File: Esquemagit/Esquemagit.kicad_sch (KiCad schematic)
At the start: 28 parts, among them J1 Conn_01x04_Pin, J2 UJ20-C-H-G-MSMT-9B-P16-TR, U1 LMV321, U2 AMS1117-3.3, U5 ESP32-WROOM-32

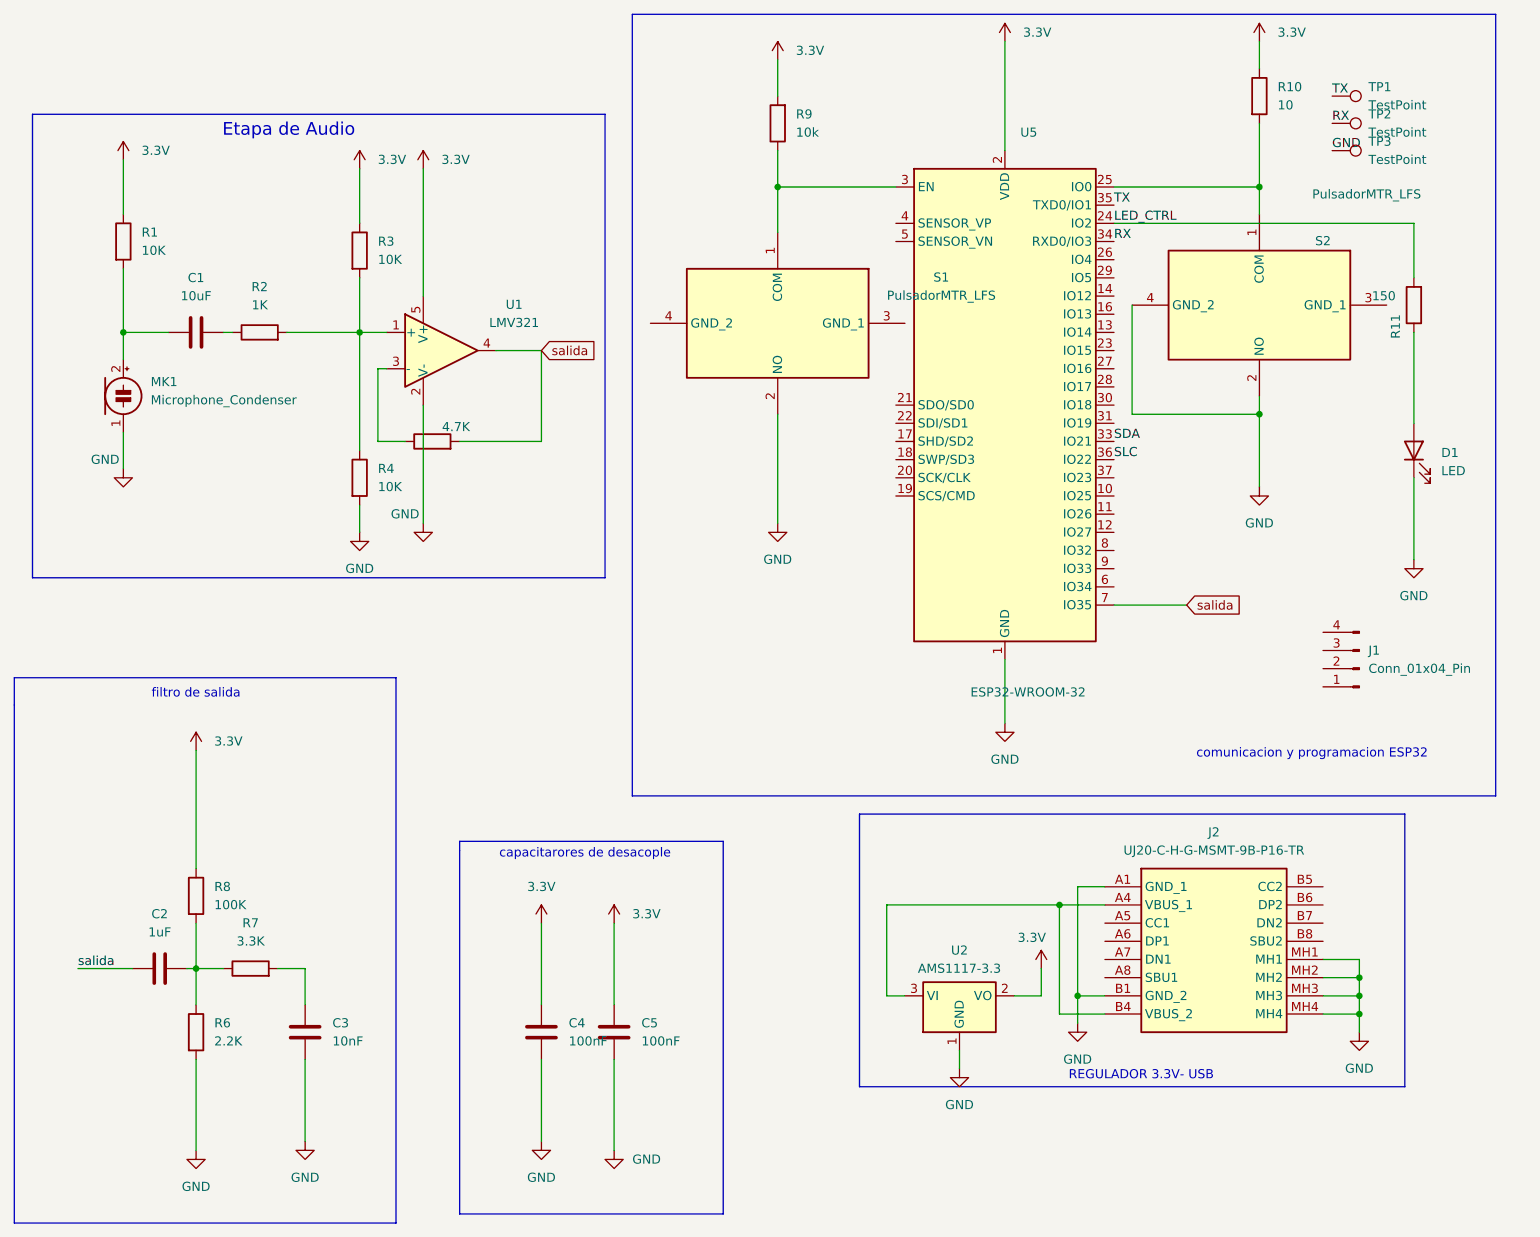
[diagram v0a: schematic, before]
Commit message: feat: pulsadores,usb c, huellas ,microfono digital
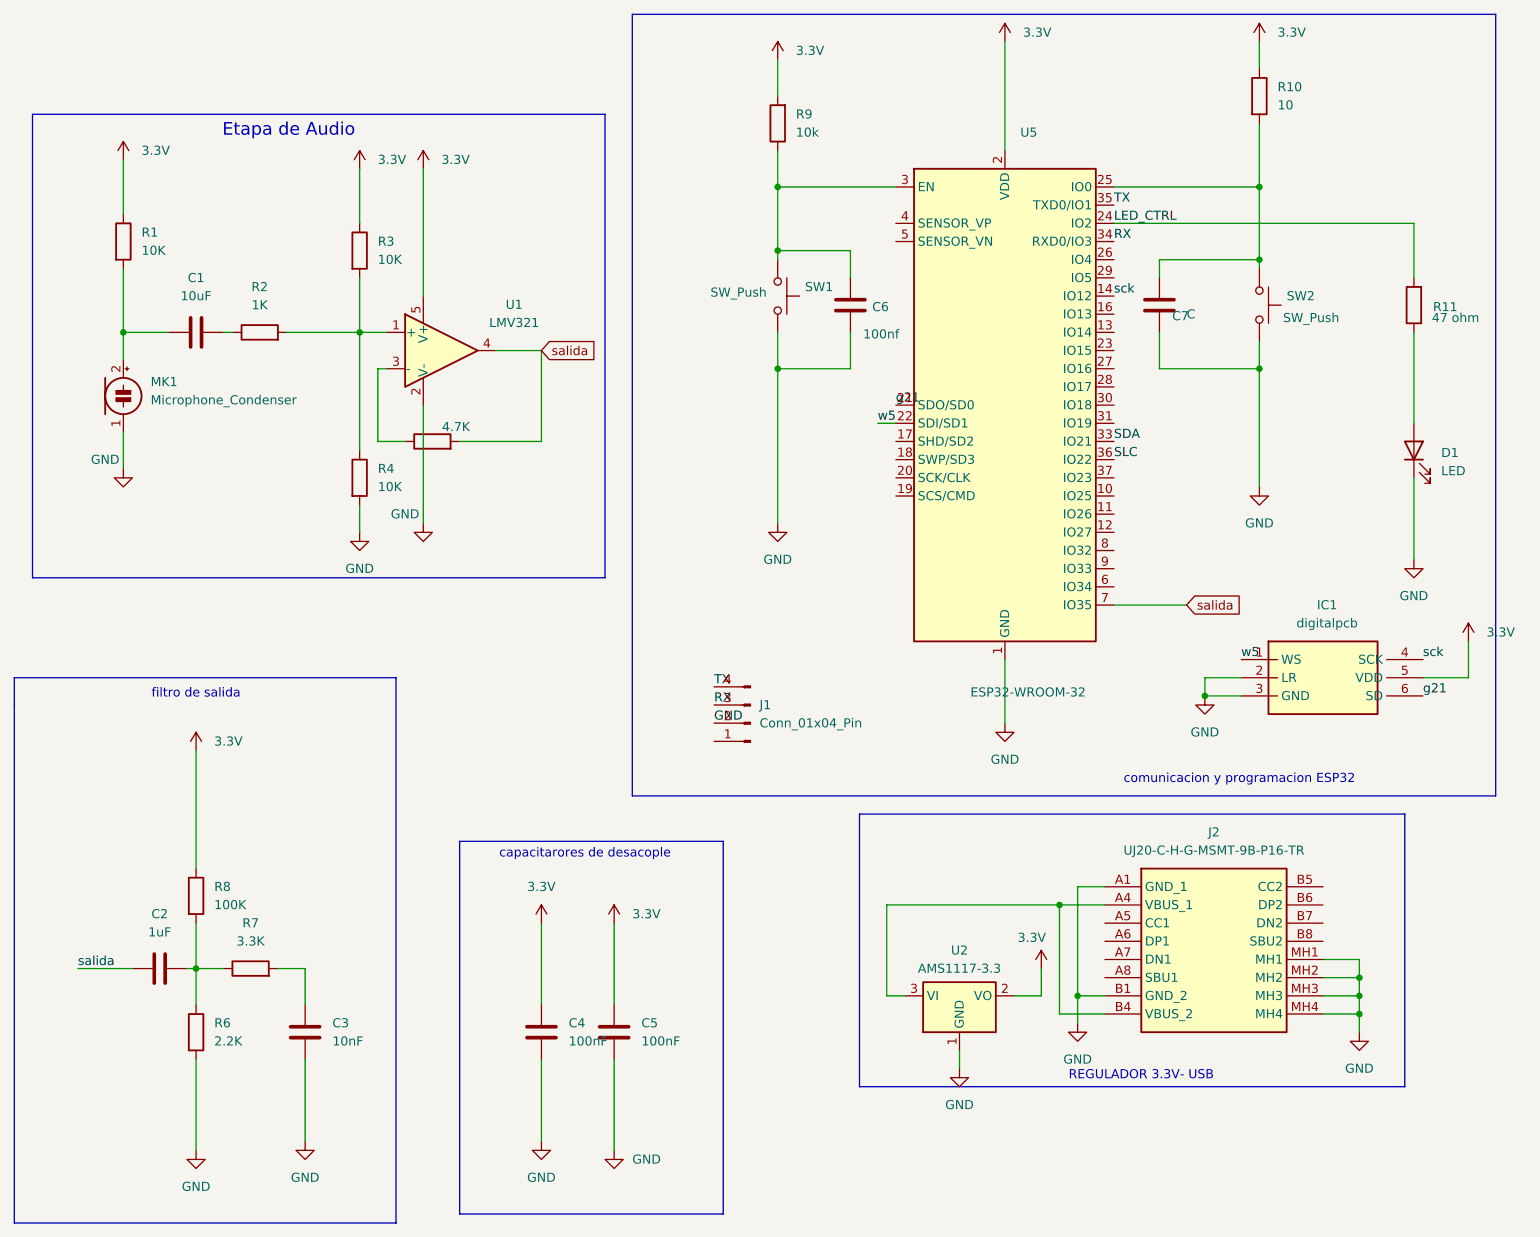
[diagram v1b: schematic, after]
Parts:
- removed S1, S2: PulsadorMTR_LFS, Button_Switch_SMD:SW_DIP_SPSTx02_Slide_6.7x6.64mm_W6.73mm_P2.54mm_LowProfile_JPin, symbol pulsador:PulsadorMTR_LFS
- removed TP1, TP2, TP3: TestPoint, TestPoint:TestPoint_Pad_D1.5mm, symbol Connector:TestPoint
- added C6: 100nf, Capacitor_SMD:C_0805_2012Metric, symbol Device:C
- added C7: C, symbol Device:C
- added IC1: digitalpcb, microfono.digital:ICS43434, symbol ICS-43434:digitalpcb
- added SW1, SW2: SW_Push, boton2:T6VJ11GQR, symbol Switch:SW_Push
- J2: footprint UJ20CHGMSMT9BP16TR -> usb.c2:UJ20CHGMSMT9BP16TR
- R11: value 150 -> 47 ohm
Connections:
- net 3.3V: now also IC1.5 (VDD)
- net GND: now also J1.2 (Pin_2), C6.2, C7.2, IC1.2 (LR), IC1.3 (GND), SW1.2, SW2.2
- net RX: now also J1.3 (Pin_3)
- net TX: now also J1.4 (Pin_4)
- net at R10.2, U5.25 (IO0): now also C7.1, SW2.1
- net at R9.1, U5.3 (EN): now also C6.1, SW1.1
- net sck: now reaches U5.14 (IO12)
- net sck: now also IC1.4 (SCK)
- net g21: now reaches U5.21 (SDO/SD0)
- net g21: now also IC1.6 (SD)
- net w5: now reaches U5.22 (SDI/SD1)
- net w5: now also IC1.1 (WS)
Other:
- moved on the sheet: J1

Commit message: feat: actualizaciones en el diseño del esquematico
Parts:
- SW1, SW2: footprint boton2:T6VJ11GQR -> Button_Switch_SMD:SW_Push_1TS009xxxx-xxxx-xxxx_6x6x5mm
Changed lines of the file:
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@@
 			)
 		)
-		(property "Footprint" "boton2:T6VJ11GQR"
+		(property "Footprint" "Button_Switch_SMD:SW_Push_1TS009xxxx-xxxx-xxxx_6x6x5mm"
 			(at 208.28 54.61 0)
 			(hide yes)
@@
 			)
 		)
-		(property "Footprint" "boton2:T6VJ11GQR"
+		(property "Footprint" "Button_Switch_SMD:SW_Push_1TS009xxxx-xxxx-xxxx_6x6x5mm"
 			(at 140.97 53.34 0)
 			(hide yes)
@@
 	)
 	(embedded_fonts no)
+	(embedded_files
+		(file
+			(name "T6VJ11GQR.kicad_mod")
+			(type other)
+			(data |KLUv/WASFAUqAIpZqA4mEHHTBswANXbbty/Vx2wuyVqXMzLR5wjB5ubmJhrevfIVAIDmCLj8AN0A
+				ygCrDdOyUs1cW9WXnMf5fncx5Xg0Fkhj1SRVJ5P13DHa9+l6qvy3qlRvr3eCRbJY/iOUXvoAI2WH
+				qW026RAiv5RST3meM+p6lKHyFcmzRsTiKSR6gqJkmERR3nFhNSIWAikZmPyGhrI4Hu0BgLKsb+1z
+				TWPy1ZTScWJ1vEcPVcL7T8Z400XCGhQUiwgXJBoRTLL0A4ACBRa/HB/59hAWScUSecgjAolYSyND
+				hEWiVOhlYkIxNNGQTEwkY5fyjMIAI8EiiXxFSxiGwQXEIsM7fEEWSeSxdOQdX4HAmjSbJhPHo6FE
+				HsMDgAACFhAeKEBcMGElLJLF0YhAlsejPQR6/Iy6J/aZDFQpbWOGr7ydHua3FtJryPtQN9NUM+lV
+				81X4DPExth9riOzv6Cu0ZpmR6pkMtmQS6u1BfZlNLyVmLm1qbFFLBiI2iE/b6zR9KzE9tcyHFlL8
+				/seMbNTq2/M5fVYd9tHbxHbOB89uSmScb4yMTUIJ3TJlpncW+zU3Z9tRzOygPyllMq1dH/RLLenx
+				8p+791JfrCHxUJKHVCwPyDBJxMIaGf7CI7IozJGXKIZeskR6Ud7RkICAtIcjgUxQWID4SEMokfcJ
+				CgcEawjEL70aEhAKNqEkkWVpFi036f4mXGwz+Z9p5Ml9bT+/F/NOgM+5ZjWahOyOux+r11Ns2i1F
+				i6jIEaG29jg/OlSNb3G6o2uYWOYvtvgYowyy1a6x4sOEegyl3m9nf0qnWO5qr8yjcyezb/np49dK
+				V2M7jMISMaCXHAZi54WO68bc4lLH61XlKsuTlGIgq20Lz0JPB8/X+J1nPXzFhzwPw4QM4sbEinSj
+				bbO6k6q/k1AdH9frdPp4Vdo0KzkhZWWUbx8z60uzevnonKZiK+/l3VoVMq3dKnVcbwUBBBBQt/Ty
+				iOBL9FISmQ0VGpZXWntAFoUh8ewxAcGesfeJTwkpLydeN/clvt6v/yH+M8Kji5HSlnCX/3VKfsyQ
+				3hrFc0yP2dBBybQ109ycdahNnX/qIS+eeuL07lzseyteCU9b9/Vaep0InTkNf1HawQWlGSgqyVvW
+				R5IFtrMvZnW2UzuU7bcW6/kvdaqlbqgDAgMNEEBAkAABBA4DFIpk0fALI0WIZUuv0CHmfcj0KHWq
+				txk3iFjPcq5j8Fi1uuSkx9Rhlwy96u7Ulotxbzc7PctvDdPzhPy+TYCpoBGhUgQhMiNCEogIBekG
+				oEhmRkzTBqHJILc3jjOIY4gCZL53tTXA+4dmJdvqsR6hxjZqxSQzKmQJSg2ut3BPoCt6npCOmWhN
+				rs/rwqLCg5WQBw4gIwNMOJE2V5IIRZBkobNBiByTHQpE071ye6dkh14wBAYsk79MtXll3fMePWoV
+				PCRAApOTbIkGlk7kMVhUuXjSIgOFM6wMoD5IPaY/RtCkJ6/YGA5g+aa5VsBjcjz5g20UgMZxYSwt
+				CFBc+C0RUm+s8rTKit6CWvwQInO+pghjKyCRA3PF1Cu9zDHNAky2tHR+t5jZOZAYaKLk0KjgpC1r
+				K8MD/l+izc4BQMe4kAaYNaLegMe1L8a0bOmdsgCRJzC2F14vhAFCAtE0YHGKEFvacITm2tBakB9D
+				NAMTJCJBDvpLhPn19QVIaQPuJAkgdxfCI1vnuEGKEprwpdzKb6LXcEkiOHU3OrKzB7OgUBibmQbb
+				WtapQHgJoujlQjiuy3o+Vgx+IUAanMrxxQfYBB6gJhgE+Fh2YqMp0ZDNVQ==|
+			)
+			(checksum "87728345582452599D8B63D97695CE93")
+		)
+	)
 )
